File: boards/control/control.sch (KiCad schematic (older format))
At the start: 91 parts, among them U1 74LV08APWJ, U10 SN74LV139APWR, U11 74LV08APWJ, U12 74LV08APWJ, U13 74LV32APWJ, U14 SN74LV00APW, U15 SN74LV139APWR, U16 74LV32APWJ, U17 SN74LV74APW, U18 SN74LV02APWR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

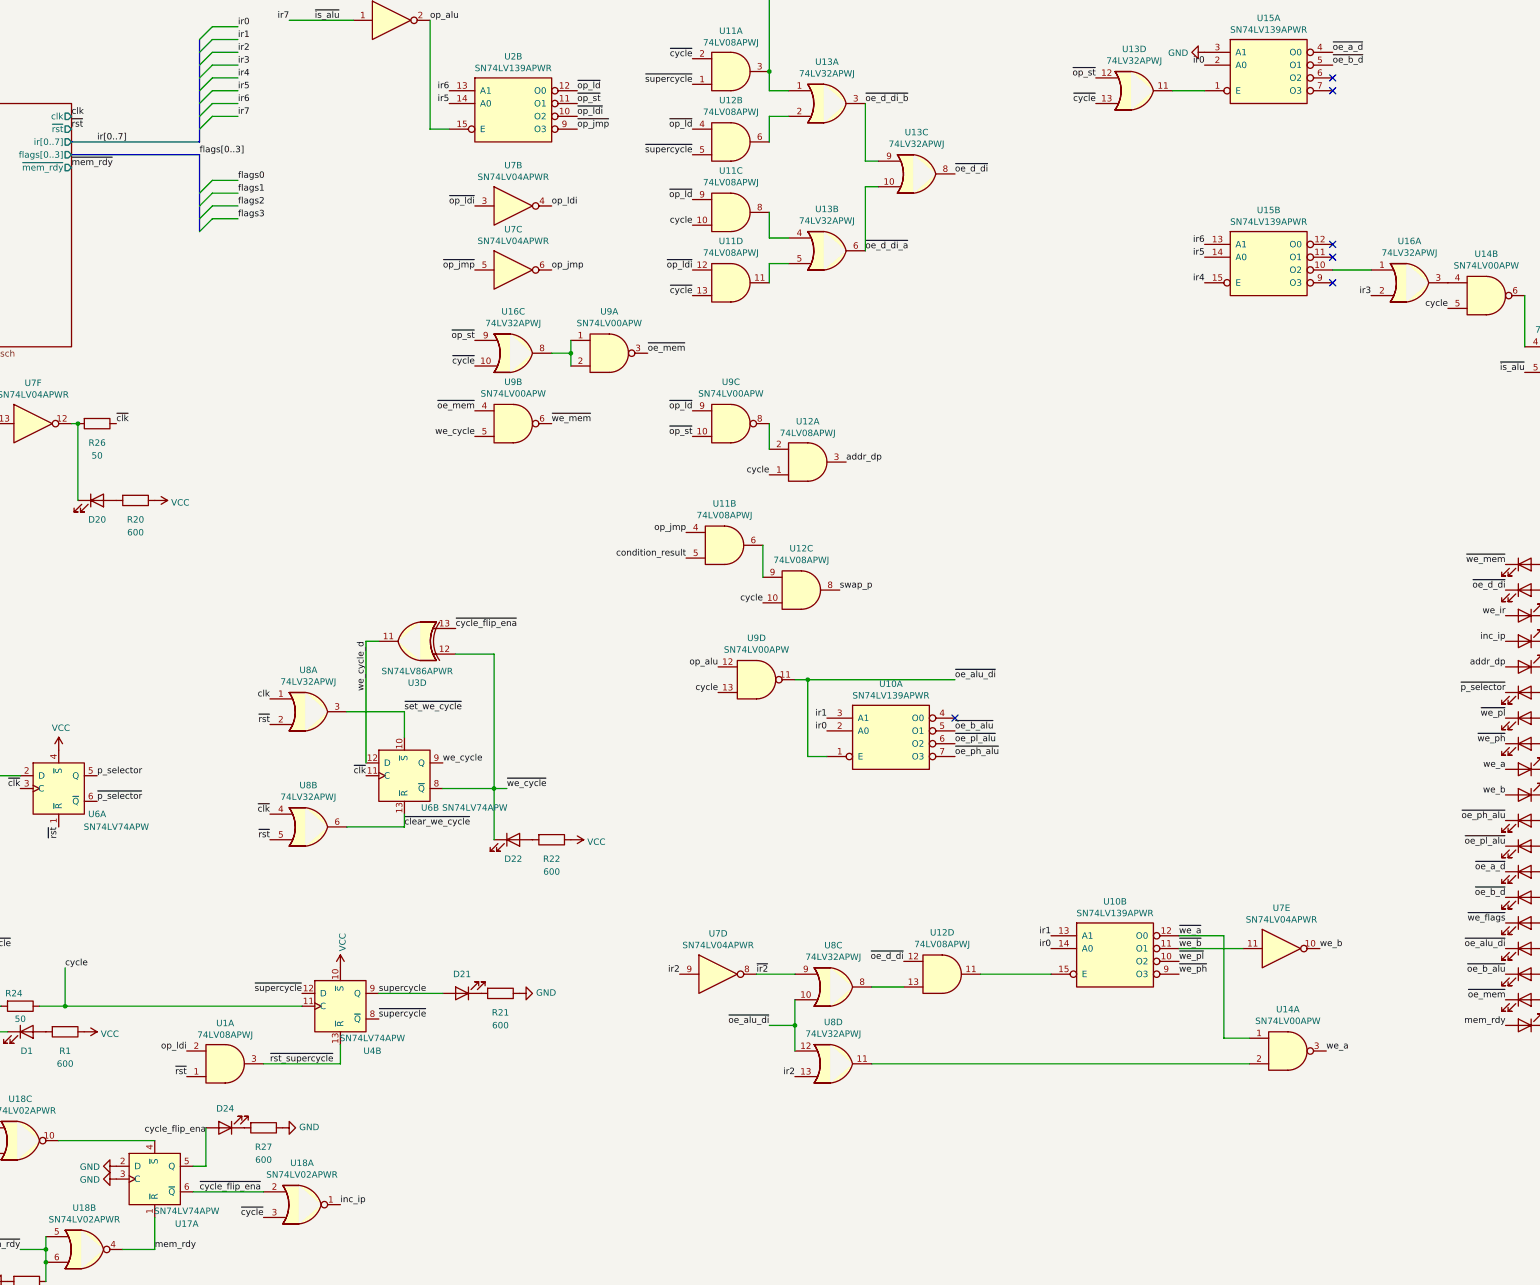
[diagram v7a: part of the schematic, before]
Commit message: Control: connect cycle_flip LED correctly
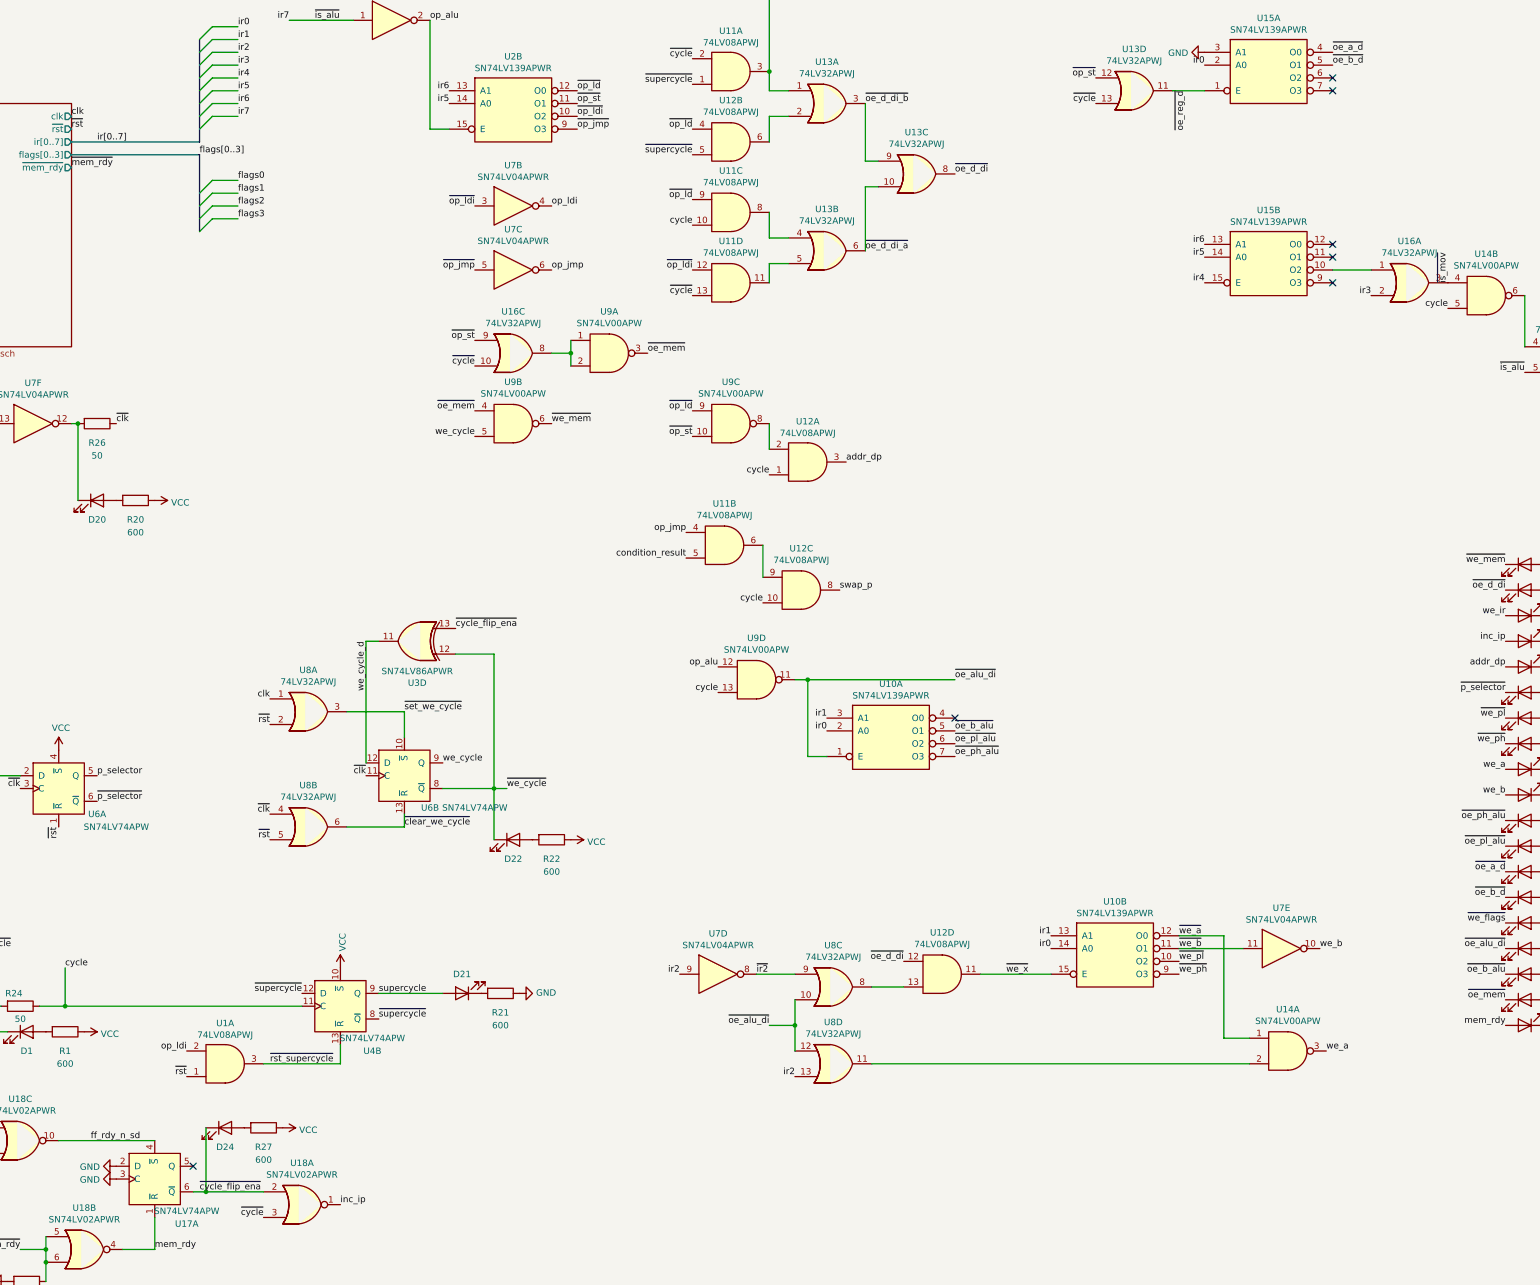
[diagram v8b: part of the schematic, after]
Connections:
- net labels added: ff_rdy_n_sd, ~is_mov, ~oe_reg_d, ~we_x
- net labels removed: cycle_flip_ena
- no-connect marks 11 -> 12
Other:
- moved on the sheet: D24
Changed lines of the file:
@@
 $EndComp
 Wire Wire Line
-	3700 10150 4250 10150
+	3700 10150 3800 10150
 Text Label 4250 10350 2    50   ~ 0
 ~cycle
@@
 F 3 "~" H 3950 9650 50  0001 C CNN
 	1    3950 9650
-	-1   0    0    1
+	1    0    0    -1
 $EndComp
 $Comp
@@
 $EndComp
 $Comp
-L power:GND #PWR0121
-U 1 1 5FDFA0FB
-P 4400 9650
-F 0 "#PWR0121" H 4400 9400 50  0001 C CNN
-F 1 "GND" V 4405 9522 50  0000 R CNN
-F 2 "" H 4400 9650 50  0001 C CNN
-F 3 "" H 4400 9650 50  0001 C CNN
-	1    4400 9650
-	0    -1   -1   0
-$EndComp
-$Comp
 L 74xx:74HC74 U17
 U 1 1 60DE8A07
@@
 $EndComp
 Wire Wire Line
-	3700 9950 3800 9950
-Wire Wire Line
-	3800 9950 3800 9650
-Text Label 3800 9700 2    50   ~ 0
-cycle_flip_ena
-Wire Wire Line
 	5650 8600 5150 8600
 $Comp
@@
 	0    -1   -1   0
 $EndComp
+NoConn ~ 3700 9950
+Wire Wire Line
+	3800 9650 3800 10150
+Connection ~ 3800 10150
+Wire Wire Line
+	3800 10150 4250 10150
 Wire Bus Line
 	3750 2050 3750 2650
 Wire Bus Line
 	3750 1150 3750 1950
+$Comp
+L power:VCC #PWR?
+U 1 1 5FE0CE0B
+P 4400 9650
+F 0 "#PWR?" H 4400 9500 50  0001 C CNN
+F 1 "VCC" V 4417 9778 50  0000 L CNN
+F 2 "" H 4400 9650 50  0001 C CNN
+F 3 "" H 4400 9650 50  0001 C CNN
+	1    4400 9650
+	0    1    1    0
+$EndComp
+Text Label 2900 9750 0    50   ~ 0
+ff_rdy_n_sd
+Text Label 10050 8450 0    50   ~ 0
+~we_x
+Text Label 11450 1550 3    50   ~ 0
+~oe_reg_d
+Text Label 13500 3050 1    50   ~ 0
+~is_mov
 $EndSCHEMATC
